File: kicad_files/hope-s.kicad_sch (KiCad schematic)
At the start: 257 parts, among them J1 EXTRA_PINS, J2 TYPE-C-31-M-12, Q1 2N7002, Q2 2N7002, Q3 2N7002, Q4 2N7002, Q5 AO3401A, Q6 2N7002, SW1 K2-1187SQ-A4SW-06, SW10 MX Switch, SW100 MX Switch, SW101 MX Switch, SW102 MX Switch, SW103 MX Switch, SW104 MX Switch, SW11 MX Switch, SW12 MX Switch, SW13 MX Switch, SW14 MX Switch, SW15 MX Switch, SW16 MX Switch, SW17 MX Switch, SW18 MX Switch, SW19 MX Switch, SW2 MX Switch, SW20 MX Switch, SW21 MX Switch, SW22 MX Switch, SW23 MX Switch, SW24 MX Switch, SW25 MX Switch, SW26 MX Switch, SW27 MX Switch, SW28 MX Switch, SW29 MX Switch, SW3 MX Switch, SW30 MX Switch, SW31 MX Switch, SW32 MX Switch, SW33 MX Switch, SW34 MX Switch, SW35 MX Switch, SW36 MX Switch, SW37 MX Switch, SW38 MX Switch, SW39 MX Switch, SW4 MX Switch, SW40 MX Switch, SW41 MX Switch, SW42 MX Switch, SW43 MX Switch, SW44 MX Switch, SW45 MX Switch, SW46 MX Switch, SW47 MX Switch, SW48 MX Switch, SW49 MX Switch, SW5 MX Switch, SW50 MX Switch, SW51 MX Switch, SW52 MX Switch, SW53 MX Switch, SW54 MX Switch, SW55 MX Switch, SW56 MX Switch, SW57 MX Switch, SW58 MX Switch, SW59 MX Switch, SW6 MX Switch, SW60 MX Switch, SW61 MX Switch, SW62 MX Switch, SW63 MX Switch, SW64 MX Switch, SW65 MX Switch, SW66 MX Switch, SW67 MX Switch, SW68 MX Switch, SW69 MX Switch, SW7 MX Switch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

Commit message: DRC ran, checks ran
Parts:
- J1: footprint acheron_Connectors:PinHeader_1x6_P2.54mm_Vertical -> acheron_Connectors:PinHeader_1x4_P2.54mm_Vertical; symbol Connector_Generic:Conn_01x06 -> Connector_Generic:Conn_01x04
- renumbered C14 to C12, C12 to C13, C13 to C14, D2 to D1, D11 to D10, D12 to D11, D13 to D12, D14 to D13, D15 to D14, D18 to D15, D17 to D16, D16 to D17, D19 to D18, D20 to D19, D3 to D2, D21 to D20, D22 to D21, D23 to D22, D24 to D23, D25 to D24, D26 to D25, D27 to D26, D28 to D27, D29 to D28, D30 to D29, D4 to D3, D31 to D30, D32 to D31, D35 to D32, D34 to D33, D33 to D34, D36 to D35, D37 to D36, D38 to D37, D39 to D38, D40 to D39, D5 to D4, D41 to D40, D42 to D41, D43 to D42, D44 to D43, D45 to D44, D46 to D45, D47 to D46, D48 to D47, D49 to D48, D66 to D49, D6 to D5, D65 to D50, D64 to D51, D50 to D52, D51 to D53, D52 to D54, D53 to D55, D54 to D56, D55 to D57, D56 to D58, D57 to D59, D7 to D6, D58 to D60, D59 to D61, D60 to D62, D61 to D63, D62 to D64, D63 to D65, D88 to D66, D8 to D7, D9 to D8, D90 to D83, D83 to D84, D84 to D85, D85 to D86, D86 to D87, D87 to D88, D10 to D9, D93 to D90, D92 to D91, D91 to D92, D1 to D93, Q5 to Q1, Q6 to Q2, Q1 to Q5, Q2 to Q6, R22 to R10, R23 to R11, R24 to R12, R20 to R13, R26 to R14, R25 to R15, R21 to R16, R27 to R17, R13 to R18, R14 to R19, R5 to R20, R6 to R21, R7 to R22, R8 to R23, R9 to R24, R10 to R25, R11 to R26, R12 to R27, R15 to R5, R16 to R6, R17 to R7, R18 to R8, R19 to R9, SW2 to SW1, SW11 to SW10, SW1 to SW104, SW12 to SW11, SW13 to SW12, SW14 to SW13, SW15 to SW14, SW16 to SW15, SW17 to SW16, SW18 to SW17, SW19 to SW18, SW20 to SW19, SW3 to SW2, SW21 to SW20, SW22 to SW21, SW23 to SW22, SW24 to SW23, SW25 to SW24, SW26 to SW25, SW27 to SW26, SW28 to SW27, SW29 to SW28, SW30 to SW29, SW4 to SW3, SW31 to SW30, SW32 to SW31, SW33 to SW32, SW34 to SW33, SW35 to SW34, SW36 to SW35, SW37 to SW36, SW38 to SW37, SW39 to SW38, SW40 to SW39, SW5 to SW4, SW41 to SW40, SW42 to SW41, SW43 to SW42, SW44 to SW43, SW45 to SW44, SW46 to SW45, SW47 to SW46, SW48 to SW47, SW49 to SW48, SW64 to SW49, SW6 to SW5, SW65 to SW50, SW66 to SW51, SW50 to SW52, SW51 to SW53, SW52 to SW54, SW53 to SW55, SW54 to SW56, SW55 to SW57, SW56 to SW58, SW57 to SW59, SW7 to SW6, SW58 to SW60, SW59 to SW61, SW60 to SW62, SW61 to SW63, SW62 to SW64, SW63 to SW65, SW92 to SW66, SW8 to SW7, SW9 to SW8, SW94 to SW87, SW87 to SW88, SW88 to SW89, SW10 to SW9, SW89 to SW90, SW90 to SW91, SW91 to SW92, SW95 to SW94, SW96 to SW95, SW97 to SW96, SW98 to SW97, SW104 to SW98
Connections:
- net E-PA0 is gone; now on net 3V3: J1.1 (Pin_1)
- net E-PA1 is gone; now on net PA9: J1.2 (Pin_2)
- net 3V3: no longer J1.3 (Pin_3)
- net 5V: now also J1.3 (Pin_3); no longer J1.5 (Pin_5)
- net C0: now also U2.11 (PA1)
- net C1: now also U2.19 (PB1)
- net C10: now also U2.2 (PC13)
- net C11: now also U2.46 (PB9)
- net C12: now also U2.38 (PA15)
- net C13: now also SW13.2, U2.45 (PB8); no longer SW13.1
- net C14: now also U2.41 (PB5)
- net C15: now also U2.40 (PB4)
- net C16: now also U2.39 (PB3)
- net C2: now also U2.21 (B10)
- net C3: now also U2.25 (PB12)
- net C4: now also U2.27 (PB14)
- net C5: now also R4.2, U2.31 (PA10)
- net C7: now also U2.29 (PA8)
- net C8: now also U2.28 (PB15)
- net C9: now also U2.3 (PC14_OSC32IN)
- net CAPS_INDICATOR: now also U2.16 (PA6)
- net GND: now also J1.4 (Pin_4); no longer J1.6 (Pin_6)
- net LED_PWM: now also U2.18 (PB0); no longer U2.19 (PB1)
- net PA9: no longer J1.4 (Pin_4)
- net R0: now also U2.12 (PA2)
- net R1: now also U2.13 (PA3)
- net R2: now also U2.14 (PA4)
- net R3: now also U2.17 (PA7)
- net R4: now also U2.26 (PB13)
- net R5: now also U2.10 (PA0-WKUP)
- net SCROLL_INDICATOR: now also U2.15 (PA5)
- net at D14.2 (A): now also SW13.1; no longer SW13.2
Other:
- note added: "INDICATORS"
- note added: "USB"
- note removed: "LED BACKLIGHT"
- note removed: "USB Connector"
- moved on the sheet: C1, C10, C11, C12, C13, C14, C2, C3, C4, C5, C6, C7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

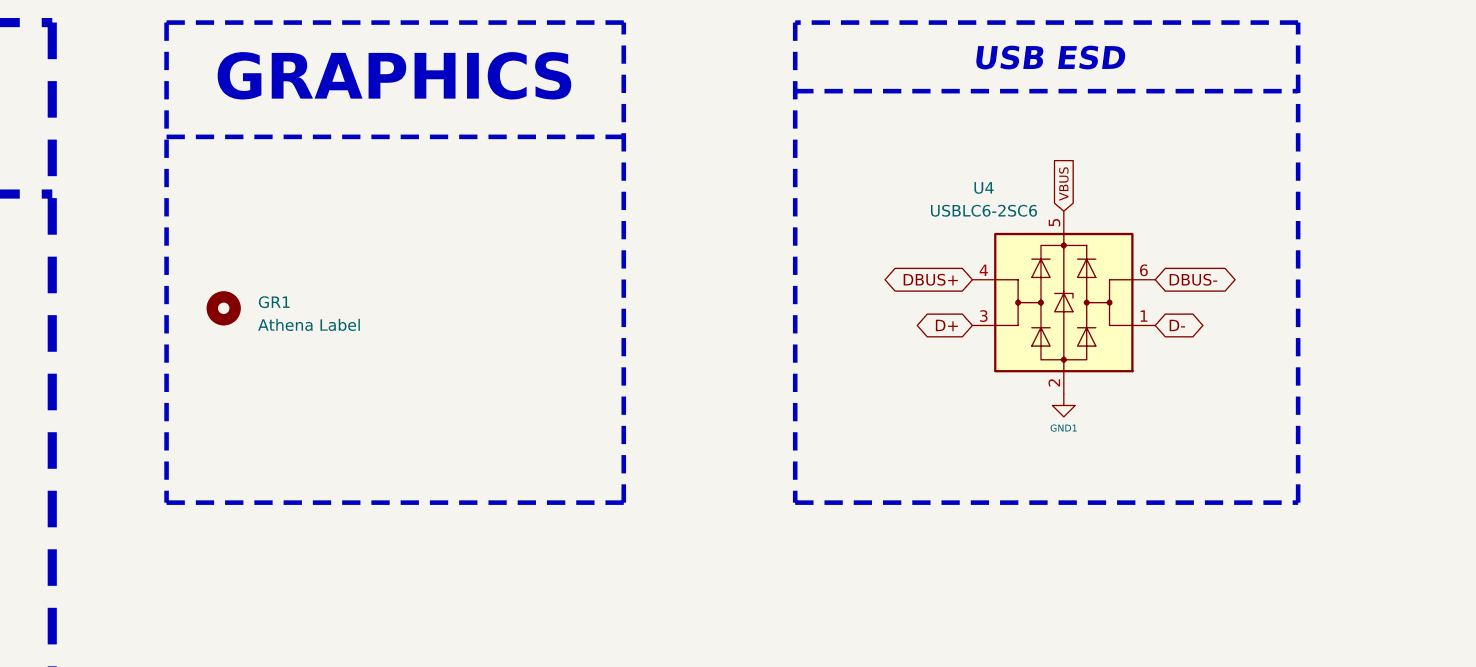
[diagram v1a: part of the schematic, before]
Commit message: Organize schematic and logos
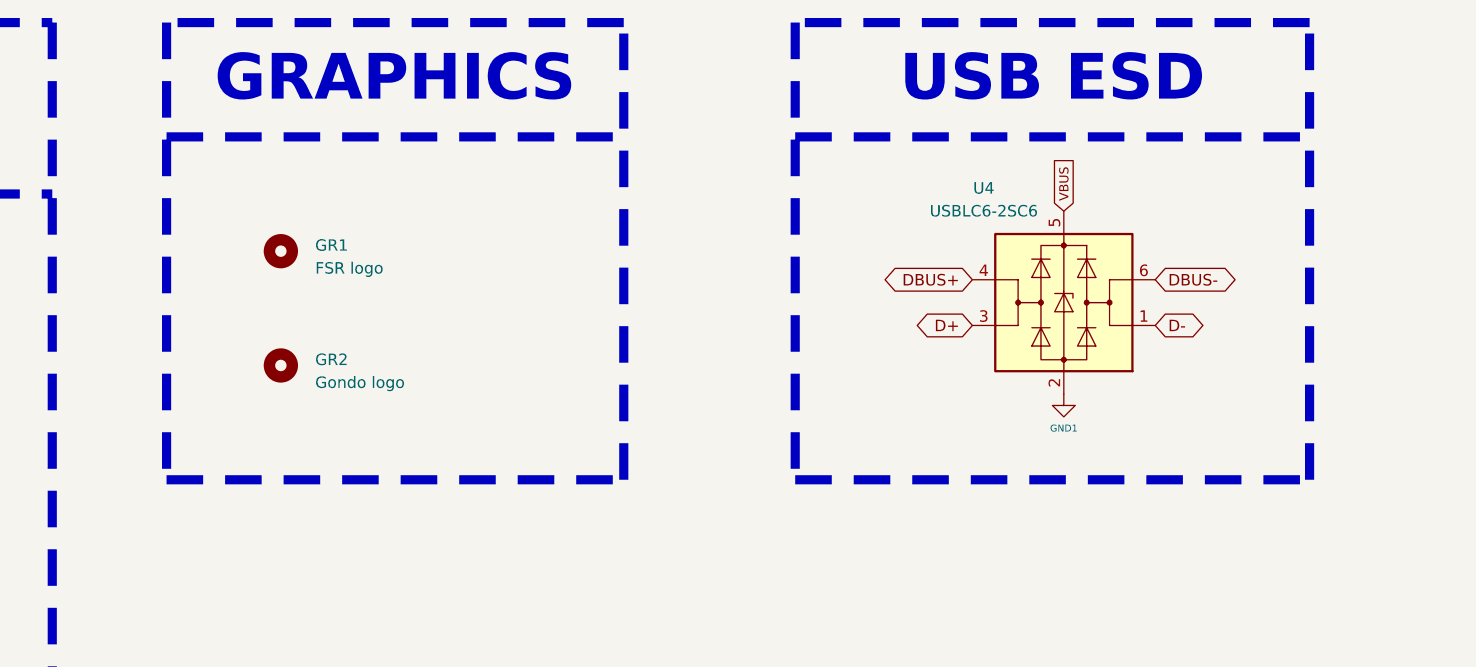
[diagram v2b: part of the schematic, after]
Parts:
- added GR2: Gondo logo, hope-lib:gondo_logo_plated, symbol Mechanical:MountingHole
- GR1: value Athena Label -> FSR logo; footprint athena_library:athena_label_35x5.6 -> hope-lib:FSR_logo
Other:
- moved on the sheet: GR1
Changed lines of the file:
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@@
 	(text "USB ESD"
 		(exclude_from_sim no)
-		(at 565.785 24.765 0)
+		(at 574.675 25.4 0)
 		(effects
 			(font
-				(size 2.54 2.54)
-				(thickness 0.508)
+				(size 5.08 5.08)
+				(thickness 1.524)
 				(bold yes)
-				(italic yes)
 			)
-			(justify left bottom)
 		)
 	)
@@
 	(polyline
 		(pts
-			(xy 476.25 19.05) (xy 476.25 72.39)
+			(xy 476.25 19.05) (xy 476.25 69.85)
 		)
 		(stroke
-			(width 0.508)
+			(width 1.016)
 			(type dash)
 		)
@@
 	(polyline
 		(pts
-			(xy 546.1 72.39) (xy 601.98 72.39)
+			(xy 546.1 69.85) (xy 603.25 69.85)
 		)
 		(stroke
-			(width 0.508)
+			(width 1.016)
 			(type dash)
 		)
@@
 	(polyline
 		(pts
-			(xy 601.98 72.39) (xy 601.98 19.05)
+			(xy 603.25 69.85) (xy 603.25 19.05)
 		)
 		(stroke
-			(width 0.508)
+			(width 1.016)
 			(type dash)
 		)
@@
 		)
 		(stroke
-			(width 0.508)
+			(width 1.016)
 			(type dash)
 		)
@@
 	(polyline
 		(pts
-			(xy 527.05 72.39) (xy 527.05 19.05)
+			(xy 527.05 69.85) (xy 527.05 19.05)
 		)
 		(stroke
-			(width 0.508)
+			(width 1.016)
 			(type dash)
 		)
@@
 	(polyline
 		(pts
-			(xy 476.25 72.39) (xy 527.05 72.39)
+			(xy 476.25 69.85) (xy 527.05 69.85)
 		)
 		(stroke
-			(width 0.508)
+			(width 1.016)
 			(type dash)
 		)
@@
 	(polyline
 		(pts
-			(xy 601.98 19.05) (xy 546.1 19.05)
+			(xy 603.25 19.05) (xy 546.1 19.05)
 		)
 		(stroke
-			(width 0.508)
+			(width 1.016)
 			(type dash)
 		)
@@
 	(polyline
 		(pts
-			(xy 546.1 19.05) (xy 546.1 72.39)
+			(xy 546.1 19.05) (xy 546.1 69.85)
 		)
 		(stroke
-			(width 0.508)
+			(width 1.016)
 			(type dash)
 		)
@@
 	(polyline
 		(pts
-			(xy 546.1 26.67) (xy 601.98 26.67)
+			(xy 546.1 31.75) (xy 603.25 31.75)
 		)
 		(stroke
-			(width 0.508)
+			(width 1.016)
 			(type dash)
 		)
@@
 		)
 		(stroke
-			(width 0.508)
+			(width 1.016)
 			(type dash)
 		)
@@
 	(symbol
 		(lib_id "Mechanical:MountingHole")
-		(at 482.6 50.8 0)
+		(at 488.95 44.45 0)
 		(unit 1)
 		(exclude_from_sim no)
@@
 		(dnp no)
 		(property "Reference" "GR1"
-			(at 486.41 50.1649 0)
+			(at 492.76 43.8149 0)
 			(effects
 				(font
@@
 			)
 		)
-		(property "Value" "Athena Label"
-			(at 486.41 52.705 0)
+		(property "Value" "FSR logo"
+			(at 492.76 46.355 0)
 			(effects
 				(font
@@
 			)
 		)
-		(property "Footprint" "athena_library:athena_label_35x5.6"
-			(at 482.6 50.8 0)
+		(property "Footprint" "hope-lib:FSR_logo"
+			(at 488.95 44.45 0)
 			(effects
 				(font
@@
 		)
 		(property "Datasheet" "~"
-			(at 482.6 50.8 0)
+			(at 488.95 44.45 0)
 			(effects
 				(font
@@
 		)
 		(property "Description" ""
-			(at 482.6 50.8 0)
+			(at 488.95 44.45 0)
 			(effects
 				(font
@@
 		)
 		(property "Package" ""
-			(at 482.6 50.8 0)
+			(at 488.95 44.45 0)
 			(effects
 				(font
@@
 		)
 		(property "Manufacturer" ""
-			(at 482.6 50.8 0)
+			(at 488.95 44.45 0)
 			(effects
 				(font
@@
 		)
 		(property "Manufacturer Part Number" ""
-			(at 482.6 50.8 0)
+			(at 488.95 44.45 0)
 			(effects
 				(font
@@
 		)
 		(property "Vendor Part Number" ""
-			(at 482.6 50.8 0)
+			(at 488.95 44.45 0)
 			(effects
 				(font
@@
 		)
 		(property "Specification" ""
-			(at 482.6 50.8 0)
+			(at 488.95 44.45 0)
 			(effects
 				(font
@@
 					(unit 1)
 				)
+			)
+		)
+	)
+	(symbol
+		(lib_id "Mechanical:MountingHole")
+		(at 488.95 57.15 0)
+		(unit 1)
+		(exclude_from_sim no)
+		(in_bom no)
+		(on_board yes)
+		(dnp no)
+		(property "Reference" "GR2"
+			(at 492.76 56.5149 0)
+			(effects
+				(font
+					(size 1.27 1.27)
+				)
+				(justify left)
+			)
+		)
+		(property "Value" "Gondo logo"
+			(at 492.76 59.055 0)
+			(effects
+				(font
+					(size 1.27 1.27)
+				)
+				(justify left)
+			)
+		)
+		(property "Footprint" "hope-lib:gondo_logo_plated"
+			(at 488.95 57.15 0)
+			(effects
+				(font
+					(size 1.27 1.27)
+				)
+				(hide yes)
+			)
+		)
+		(property "Datasheet" "~"
+			(at 488.95 57.15 0)
+			(effects
+				(font
+					(size 1.27 1.27)
+				)
+				(hide yes)
+			)
+		)
+		(property "Description" ""
+			(at 488.95 57.15 0)
+			(effects
+				(font
+					(size 1.27 1.27)
+				)
+				(hide yes)
+			)
+		)
+		(property "Package" ""
+			(at 488.95 57.15 0)
+			(effects
+				(font
+					(size 1.27 1.27)
+				)
+				(hide yes)
+			)
+		)
+		(property "Manufacturer" ""
+			(at 488.95 57.15 0)
+			(effects
+				(font
+					(size 1.27 1.27)
+				)
+				(hide yes)
+			)
+		)
+		(property "Manufacturer Part Number" ""
+			(at 488.95 57.15 0)
+			(effects
+				(font
+					(size 1.27 1.27)
+				)
+				(hide yes)
+			)
+		)
+		(property "Vendor Part Number" ""
+			(at 488.95 57.15 0)
+			(effects
+				(font
+					(size 1.27 1.27)
+				)
+				(hide yes)
+			)
+		)
+		(property "Specification" ""
+			(at 488.95 57.15 0)
+			(effects
+				(font
+					(size 1.27 1.27)
+				)
+				(hide yes)
+			)
+		)
+		(instances
+			(project "hope-s"
+				(path "/9ce6b20d-0a6c-402a-b232-5eafd6242eb3"
+					(reference "GR2")
+					(unit 1)
+				)

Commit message: Release version, small corrections
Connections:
- net C3: no longer SW72.1
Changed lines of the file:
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@@
 	)
 	(junction
-		(at 196.85 207.01)
-		(diameter 0.9144)
-		(color 0 0 0 0)
-	)
-	(junction
 		(at 438.15 215.9)
 		(diameter 0)
@@
 	)
 	(junction
-		(at 133.35 368.3)
-		(diameter 0)
-		(color 0 0 0 0)
-	)
-	(junction
 		(at 601.345 240.03)
 		(diameter 0)
@@
 	)
 	(junction
-		(at 158.75 368.3)
-		(diameter 0)
-		(color 0 0 0 0)
-	)
-	(junction
 		(at 133.35 330.2)
 		(diameter 1.016)
@@
 	)
 	(junction
-		(at 184.15 368.3)
-		(diameter 0)
-		(color 0 0 0 0)
-	)
-	(junction
 		(at 158.75 82.55)
 		(diameter 1.016)
@@
 	)
 	(junction
-		(at 187.96 215.9)
-		(diameter 0.9144)
-		(color 0 0 0 0)
-	)
-	(junction
 		(at 120.65 304.8)
 		(diameter 1.016)
@@
 	(wire
 		(pts
-			(xy 189.23 217.17) (xy 187.96 217.17)
-		)
-		(stroke
-			(width 0)
-			(type solid)
-		)
-	)
-	(wire
-		(pts
 			(xy 273.05 355.6) (xy 273.05 359.41)
 		)
@@
 	(wire
 		(pts
-			(xy 158.75 368.3) (xy 158.75 370.84)
-		)
-		(stroke
-			(width 0)
-			(type solid)
-		)
-	)
-	(wire
-		(pts
 			(xy 438.15 292.1) (xy 441.96 292.1)
 		)
@@
 	(wire
 		(pts
-			(xy 133.35 368.3) (xy 137.16 368.3)
-		)
-		(stroke
-			(width 0)
-			(type solid)
-		)
-	)
-	(wire
-		(pts
 			(xy 57.15 215.9) (xy 60.96 215.9)
 		)
@@
 		)
 	)
-	(wire
-		(pts
-			(xy 133.35 368.3) (xy 133.35 370.84)
-		)
-		(stroke
-			(width 0)
-			(type solid)
-		)
-	)
 	(polyline
 		(pts
@@
 	(wire
 		(pts
-			(xy 187.96 217.17) (xy 187.96 215.9)
-		)
-		(stroke
-			(width 0)
-			(type solid)
-		)
-	)
-	(wire
-		(pts
 			(xy 588.645 245.745) (xy 588.645 246.38)
 		)
@@
 	(wire
 		(pts
-			(xy 198.12 207.01) (xy 196.85 207.01)
-		)
-		(stroke
-			(width 0)
-			(type solid)
-		)
-	)
-	(wire
-		(pts
 			(xy 273.05 228.6) (xy 247.65 228.6)
 		)
@@
 		)
 	)
-	(wire
-		(pts
-			(xy 198.12 208.28) (xy 198.12 207.01)
-		)
-		(stroke
-			(width 0)
-			(type solid)
-		)
-	)
 	(polyline
 		(pts
@@
 		)
 	)
-	(wire
-		(pts
-			(xy 184.15 368.3) (xy 184.15 370.84)
-		)
-		(stroke
-			(width 0)
-			(type solid)
-		)
-	)
